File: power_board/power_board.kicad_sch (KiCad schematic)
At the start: 45 parts, among them J1 USB-C receptacle (input from 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, J2 USB-C receptacle (5 V to Pi), J3 Lidar 15 V (pluggable 3.5 mm), J4 Momentary LED button (JST-XH 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, J5 To Pi GPIO (JST-PH 10), U1 CH224Q, U2 TBD: LTC2955 or MAX16150, U3 TPS56637RPA, U4 TPS26631PWP, U5 INA226 (addr 0x40)

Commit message: Power board: latching-switch soft power (no controller IC), CH224A, full USB-C pads, first board placement (4-layer, GND planes)
Co-Authored-By: Claude Opus 5.5 <noreply@anthropic.com>
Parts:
- removed C14: 1u 25V, Capacitor_SMD:C_0805_2012Metric, symbol pb:C
- removed U1: CH224Q, symbol pb:CH224Q
- removed U2: TBD: LTC2955 or MAX16150, symbol pb:SOFT_POWER
- added D4, D5: BAT54WS, Diode_SMD:D_SOD-323, symbol pb:D
- added R17: 1k, Resistor_SMD:R_0603_1608Metric, symbol pb:R
- added R18: 100k 1%, Resistor_SMD:R_0603_1608Metric, symbol pb:R
- added R19: 27k 1%, Resistor_SMD:R_0603_1608Metric, symbol pb:R
- added R20, R22: 100k, Resistor_SMD:R_0603_1608Metric, symbol pb:R
- added R21: 10k, Resistor_SMD:R_0603_1608Metric, symbol pb:R
- added U1: CH224A, Package_SO:SSOP-10-1EP_3.9x4.9mm_P1mm_EP2.1x3.3mm, symbol pb:CH224A
- C1: Note U1 VHV -> (none)
- C10: Note eFuse Cin -> (none)
- C11: Note soft-start -> (none)
- C12: Note eFuse Cout -> (none)
- C13: Note INA226 VS -> (none)
- C2, C3: Note buck Cin -> (none)
- C4: Note buck Cin HF -> (none)
- C5: Note bootstrap -> (none)
- C6, R5: Note feed-forward (optional) -> (none)
- C7, C8, C9: Note buck Cout -> (none)
- D1: Note TVS -> (none)
- D2: Note 5 V on (K=1, A=2) -> (none)
- D3: Note lidar on (K=1, A=2) -> (none)
- F1: Note bank cuts out ~3 A anyway -> (none)
- J3: footprint TerminalBlock_Phoenix:TerminalBlock_Phoenix_MPT-0,5-2-2.54_1x02_P2.54mm_Horizontal -> Connector_Phoenix_MC:PhoenixContact_MC_1,5_2-G-3.5_1x02_P3.50mm_Horizontal
- J4: value Momentary LED button (JST-XH 4) -> Latching 16 mm LED button (JST-XH 4)
- L1: footprint Inductor_SMD:L_Vishay_IHLP-2525 -> Inductor_SMD:L_Vishay_IHLP-3232; Note IHLP-3232DZ-3R3 class -> (none)
- R1: Note INA226 shunt -> (none)
- R12: Note ILIM 2.0 A -> (none)
- R13: Note lidar default OFF -> (none)
- R15: Note ~2 mA at 15 V -> (none)
- R16: value 1k -> 0R; Note button ring LED -> (none)
- R2: Note CH224Q CFG1: 15 V -> (none)
- R3: Note FB top: 5.10 V -> (none)
- R4: Note FB bottom -> (none)
- R6: Note PG pull-up -> (none)
- R7, R8: Note Rp -> (none)
- R9: Note UVLO 10.0 V / OVP 20.0 V -> (none)
- U3: footprint (none) -> power_board:TI_RPA0010A_PLACEHOLDER
- U4: footprint Package_SO:HTSSOP-20-1EP_4.4x6.5mm_P0.65mm_EP3.4x6.5mm -> Package_SO:HTSSOP-20-1EP_4.4x6.5mm_P0.65mm_EP3.4x6.5mm_Mask2.96x2.96mm_ThermalVias
- U5: footprint Package_SO:VSSOP-10_3x3mm_P0.5mm -> Package_SO:MSOP-10_3x3mm_P0.5mm
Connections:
- net BUCK_EN: now also D4.1, D5.1, R20.1
- net GND: now also J1.A12 (GND), J1.B1 (GND), J1.B12 (GND), J1.SH (GND), J2.A12 (GND), J2.B1 (GND), J2.B12 (GND), J2.SH (GND), R19.2, R20.2, R22.2, U1.11 (GND); no longer J1.S1 (SHIELD), J2.S1 (SHIELD), J4.2 (SW_B)
- net IN_CC1: now also U1.7 (CC1)
- net IN_CC2: now also U1.6 (CC2)
- net IN_DM: now also J1.B7 (D-), U1.5 (DM)
- net IN_DP: now also J1.B6 (D+), U1.4 (DP)
- net PD_CFG1: now also U1.9 (CFG1)
- net PD_PG_N: now also U1.10 (PG)
- net V15: now also R17.1
- net V5: now also J2.A9 (VBUS), J2.B4 (VBUS), J2.B9 (VBUS)
- net VBUS_RAW: now also J1.A9 (VBUS), J1.B4 (VBUS), J1.B9 (VBUS), U1.1 (VHV), U1.8 (VBUS)
- net BTN renamed SW_FEED
- net SW_FEED: now also R17.2
- net KILL renamed KEEP_ALIVE
- net KEEP_ALIVE: now also D5.2, R22.1
- net SHDN_REQ renamed SW_SENSE
- net SW_SENSE: now also R21.2
- new net SW_ON: J4.2 (SW_NO), R18.1
- new net SW_TAP: D4.2, R18.2, R19.1, R21.1
- no-connect marks 7 -> 17

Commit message: Power board: TPS56637 RPA0010A footprint from the datasheet land pattern, upright 46x60 board for the buck bay, USB-C on the top edge, top-entry lidar terminal, button LED from the switch
Co-Authored-By: Claude Opus 5.5 <noreply@anthropic.com>
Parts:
- J3: footprint Connector_Phoenix_MC:PhoenixContact_MC_1,5_2-G-3.5_1x02_P3.50mm_Horizontal -> Connector_Phoenix_MC:PhoenixContact_MCV_1,5_2-G-3.5_1x02_P3.50mm_Vertical
- R17: value 1k -> 100R 1206; footprint Resistor_SMD:R_0603_1608Metric -> Resistor_SMD:R_1206_3216Metric
- U3: footprint power_board:TI_RPA0010A_PLACEHOLDER -> power_board:TI_RPA0010A
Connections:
- net SW_ON: now also R16.1
- net V5: no longer R16.1

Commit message: Power board: TI RPA0010A footprint (Ultra Librarian, fingers fixed to pad 8), buck placed per datasheet layout guide, input chain in signal order
Co-Authored-By: Claude Opus 5.5 <noreply@anthropic.com>
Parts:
- U3: footprint power_board:TI_RPA0010A -> power_board:RPA0010A

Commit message: Power board: fully routed (hand-routed power + Kelvin sense, In1 GND / In2 V15 planes, fan-out vias, Freerouting for signals), DRC clean; build_all.ps1 and export_fab.ps1
Co-Authored-By: Claude Opus 5.5 <noreply@anthropic.com>
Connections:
- removed net IN_DM: J1.A7 (D-), J1.B7 (D-), U1.5 (DM)
- removed net IN_DP: J1.A6 (D+), J1.B6 (D+), U1.4 (DP)
- no-connect marks 17 -> 23

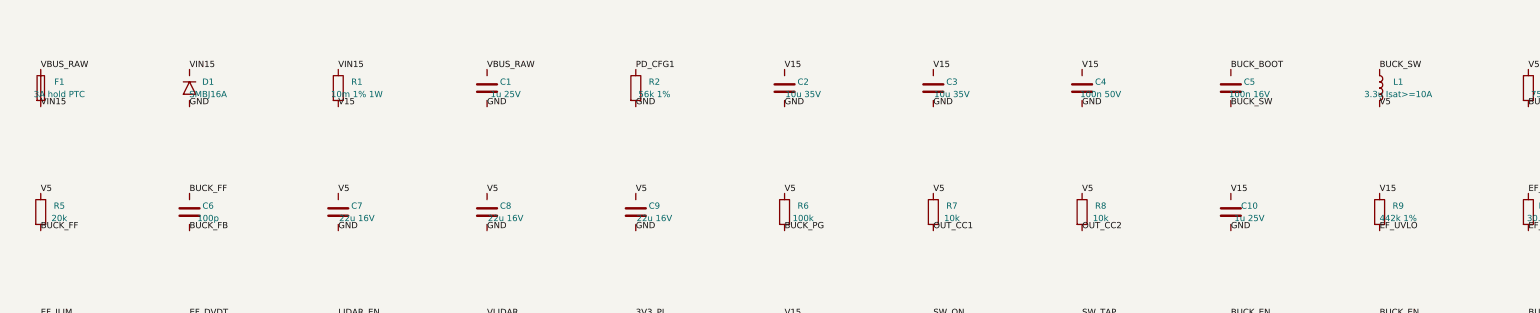
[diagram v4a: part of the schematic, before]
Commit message: Power board: in-stock parts (MDA7050 inductor, 2920 PTC, Kefa terminal, uprated 1210 caps), D+/D- dropped, input sense block shifted for the fuse; DRC 0 violations; JLC BOM/CPL generator
Co-Authored-By: Claude Opus 5.5 <noreply@anthropic.com>
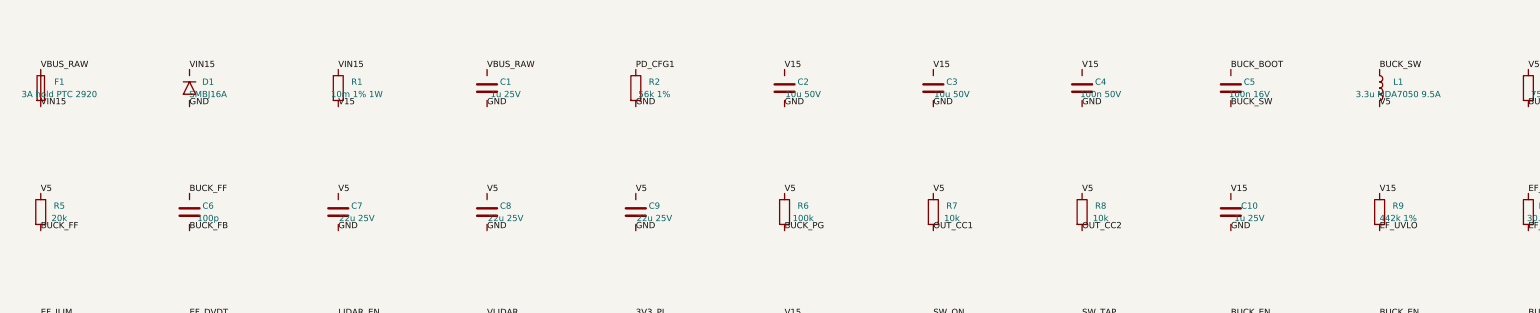
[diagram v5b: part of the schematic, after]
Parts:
- C2, C3: value 10u 35V -> 10u 50V
- C7, C8, C9: value 22u 16V -> 22u 25V
- F1: value 3A hold PTC -> 3A hold PTC 2920; footprint Fuse:Fuse_1812_4532Metric -> Fuse:Fuse_2920_7451Metric
- L1: value 3.3u Isat>=10A -> 3.3u MDA7050 9.5A; footprint Inductor_SMD:L_Vishay_IHLP-3232 -> Inductor_SMD:L_KOHERelec_MDA7030

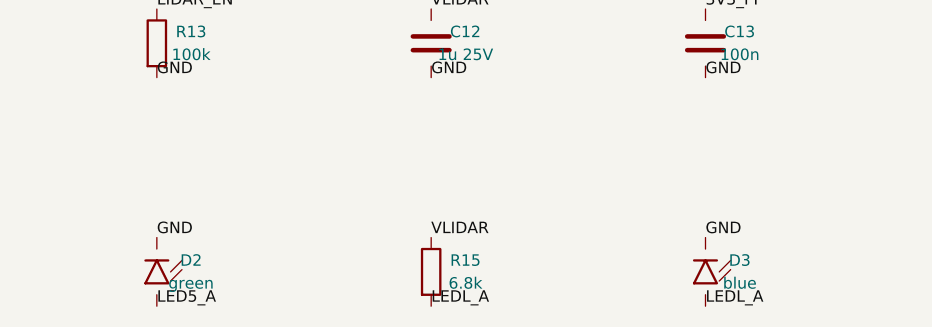
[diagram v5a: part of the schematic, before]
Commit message: Power board: HRO TYPE-C-31-M-12 sockets (in stock), KT-0603R/W Basic LEDs, FMF25 shunt; CC traces between the shell pads
Co-Authored-By: Claude Opus 5.5 <noreply@anthropic.com>
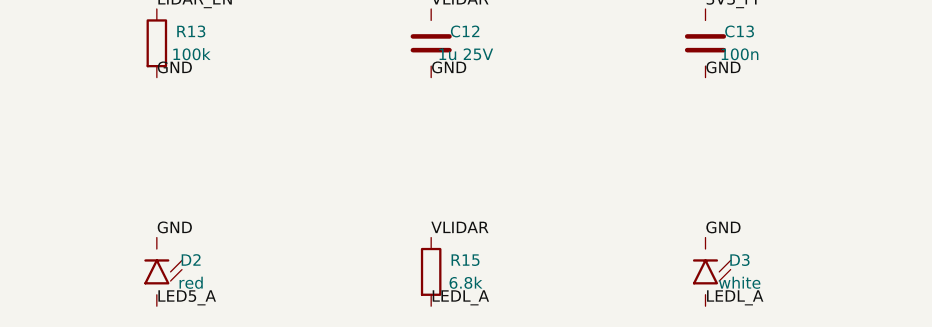
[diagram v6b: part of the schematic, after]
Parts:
- D2: value green -> red
- D3: value blue -> white
- J1, J2: footprint Connector_USB:USB_C_Receptacle_GCT_USB4105-xx-A_16P_TopMnt_Horizontal -> Connector_USB:USB_C_Receptacle_HRO_TYPE-C-31-M-12
